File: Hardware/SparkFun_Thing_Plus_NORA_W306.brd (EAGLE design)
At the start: 22.9 x 58.4 mm, 155 parts, among them J1 THING_PLUS_LOGICAL, J2 LiPo, J3 QWIIC_RA, J4 MICRO-SDFRICTION, J5 USB-C, J6 SWD (DNP), Q1 3.1A/30V/105mΩ, Q2 MBT3904DW1T1, U1 UBLOX_NORA_W306, U3 XC6222B331MR-G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

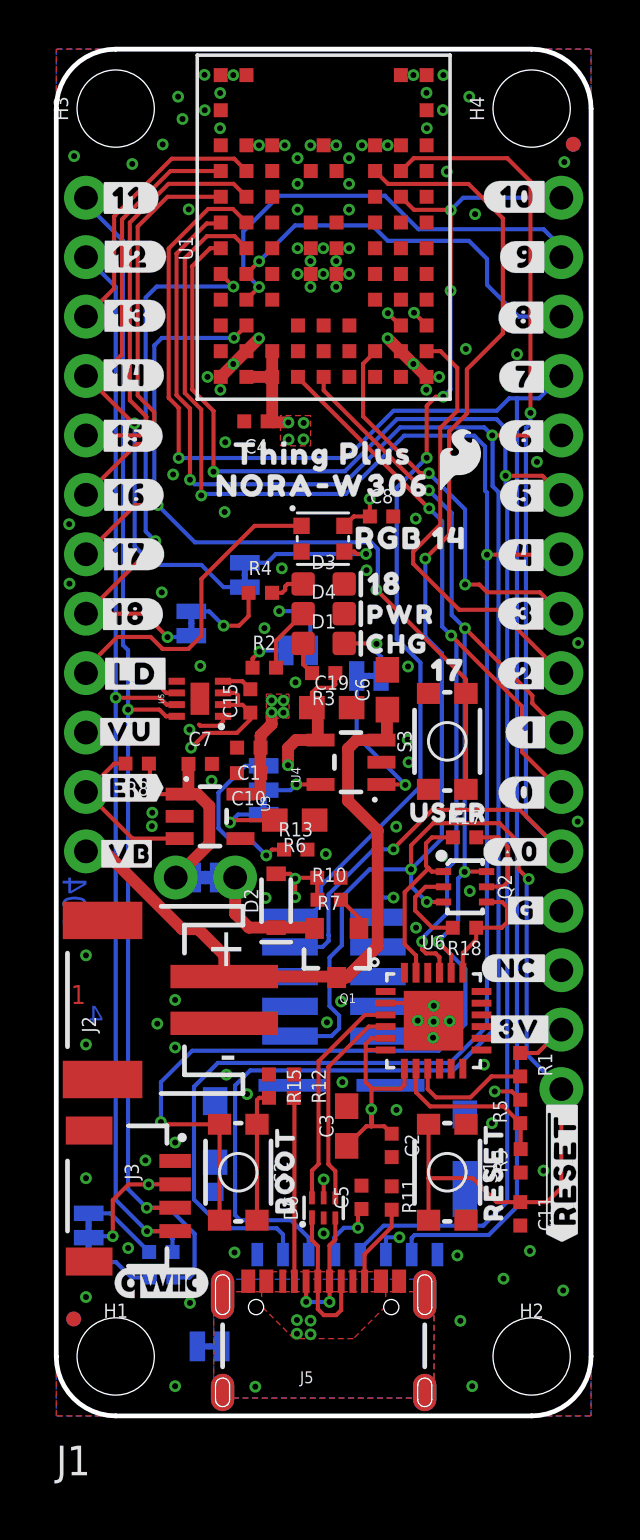
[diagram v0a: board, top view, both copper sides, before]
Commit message: Moved SDA/SCL from inner to bottom layer
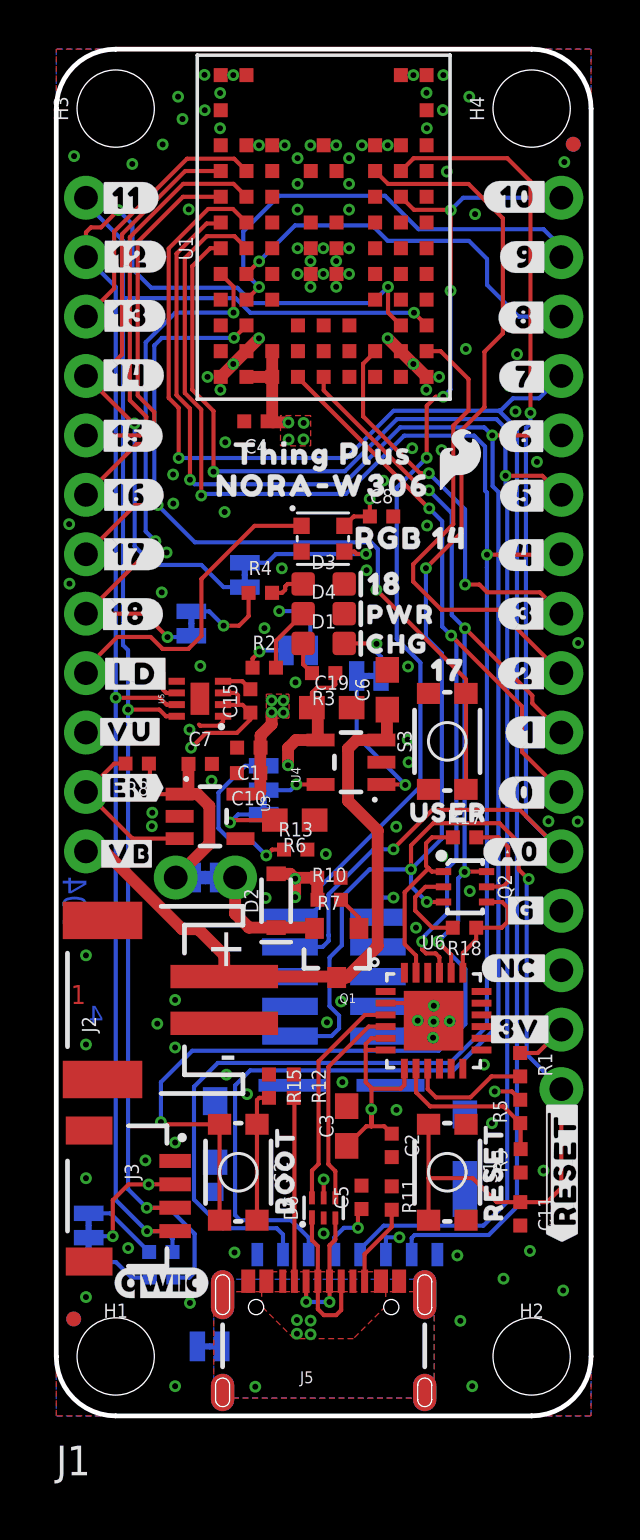
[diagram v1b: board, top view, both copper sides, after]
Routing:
- net PA26/SDA: track 70.6 -> 66.3 mm
- net PA25/SCL: track 63.5 -> 67.8 mm, vias 3 -> 4
- net PA30: track 19.0 -> 19.9 mm
- net GND: vias 118 -> 125

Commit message: Removed V_BUS plane on inner layer
To avoid splitting up the 3.3V plane on the inner layer, I decided to route V_USB (instead of using an additional separate plane).
Added some stitching traces/polys to stich up the 3.3V plane.
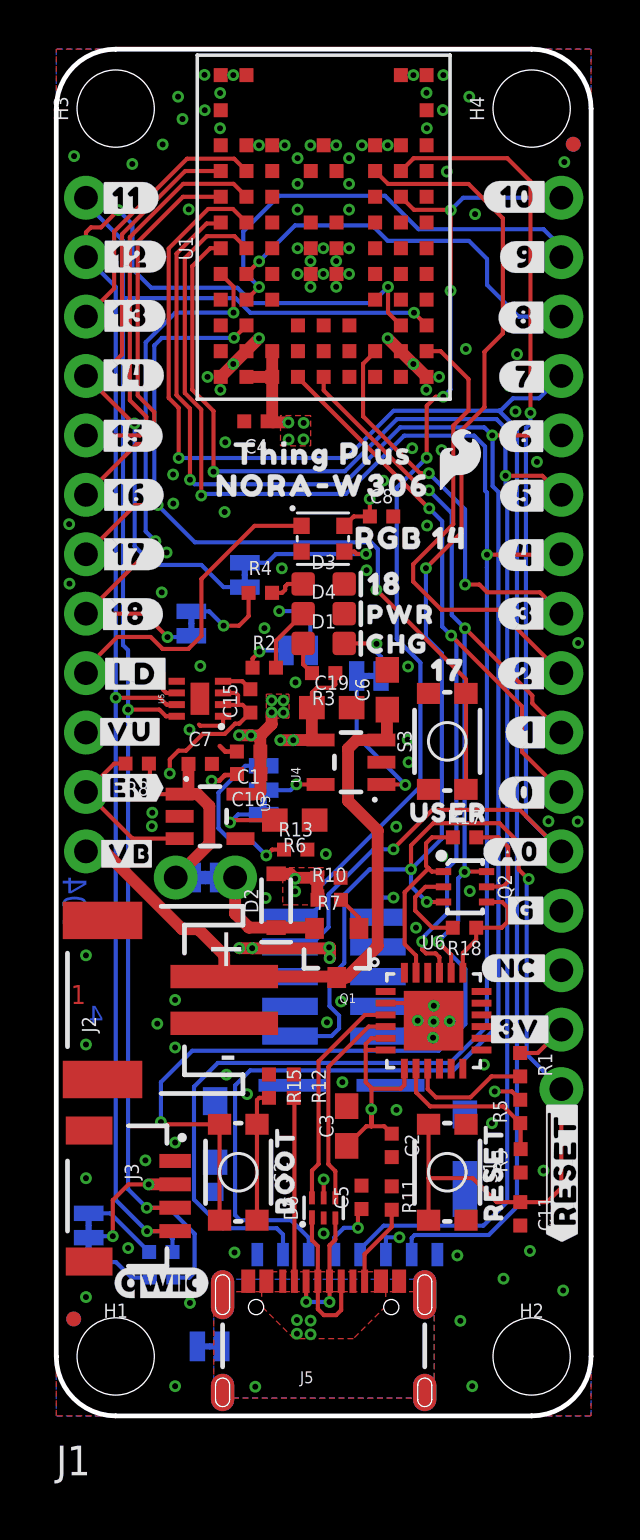
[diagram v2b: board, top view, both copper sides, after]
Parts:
- moved C1 0.17 mm to (8.22, 28.4)
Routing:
- net V_USB: track 19.8 -> 55.8 mm, vias 9 -> 10
- net 3.3V: track 46.3 -> 42.3 mm, vias 15 -> 21
- net GND: track 11.5 -> 13.6 mm

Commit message: Updated to new 0603 RED LED
-also updated the limiting resistor to correct value (4.7K) for DIO-17976
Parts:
- R2: value 1k -> 4.7k
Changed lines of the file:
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@@
 <setting verticaltext="up"/>
 </settings>
-<grid distance="0.05" unitdist="inch" unit="inch" style="lines" multiple="1" display="yes" altdistance="0.0001" altunitdist="inch" altunit="inch"/>
+<grid distance="0.05" unitdist="inch" unit="inch" style="lines" multiple="1" display="yes" altdistance="0.005" altunitdist="inch" altunit="inch"/>
 <layers>
 <layer number="1" name="Top" color="4" fill="1" visible="yes" active="yes"/>
@@
 <layer number="98" name="Guide" color="6" fill="1" visible="no" active="no"/>
 <layer number="99" name="SpiceOrder" color="7" fill="1" visible="no" active="no"/>
-<layer number="100" name="Muster" color="7" fill="1" visible="no" active="yes"/>
+<layer number="100" name="Muster" color="7" fill="1" visible="yes" active="yes"/>
 <layer number="101" name="Patch_Top" color="12" fill="4" visible="no" active="no"/>
 <layer number="102" name="Vscore" color="7" fill="1" visible="no" active="no"/>
@@
 <attribute name="VALUE" x="6.5532" y="4.1148" size="0.6096" layer="28" font="vector" ratio="20" rot="MR180" align="top-center"/>
 </element>
-<element name="R2" library="SparkFun-Resistors" package="0402-TIGHT" value="1k" x="8.89" y="31.981140625" smashed="yes">
+<element name="R2" library="SparkFun-Resistors" package="0402-TIGHT" value="4.7k" x="8.89" y="31.981140625" smashed="yes">
 <attribute name="NAME" x="8.89" y="32.743140625" size="0.6096" layer="25" font="vector" ratio="20" align="bottom-center"/>
-<attribute name="PROD_ID" value="RES-14342" x="8.89" y="31.981140625" size="1.778" layer="27" font="vector" ratio="15" display="off"/>
-<attribute name="VALUE" value="1k" x="8.89" y="31.219140625" size="0.6096" layer="27" font="vector" ratio="20" align="top-center"/>
+<attribute name="PROD_ID" value="RES-15343" x="8.89" y="31.981140625" size="1.778" layer="27" font="vector" ratio="15" display="off"/>
+<attribute name="VALUE" value="4.7k" x="8.89" y="31.219140625" size="0.6096" layer="27" font="vector" ratio="20" align="top-center"/>
 </element>
 <element name="LED" library="SparkFun-Jumpers" package="SMT-JUMPER_2_NC_TRACE_SILK" package3d_urn="urn:adsk.eagle:package:39281/1" value="" x="10.337803125" y="32.720278125" smashed="yes" rot="MR0">
@@
 <element name="D4" library="SparkFun-LED" package="LED-0603" value="RED" x="11.43" y="34.29" smashed="yes">
 <attribute name="NAME" x="11.43" y="34.925" size="0.6096" layer="25" font="vector" ratio="20" align="bottom-center"/>
-<attribute name="PROD_ID" value="DIO-00819" x="11.43" y="34.29" size="1.778" layer="27" font="vector" ratio="15" display="off"/>
-<attribute name="VALUE" x="11.43" y="33.655" size="0.6096" layer="27" font="vector" ratio="20" align="top-center"/>
+<attribute name="PROD_ID" value="DIO-17976" x="11.43" y="34.29" size="1.778" layer="27" font="vector" ratio="15" display="off"/>
 </element>
 <element name="U$23" library="output" package="PWR0" value="" x="14.72691875" y="34.25190625" smashed="yes"/>

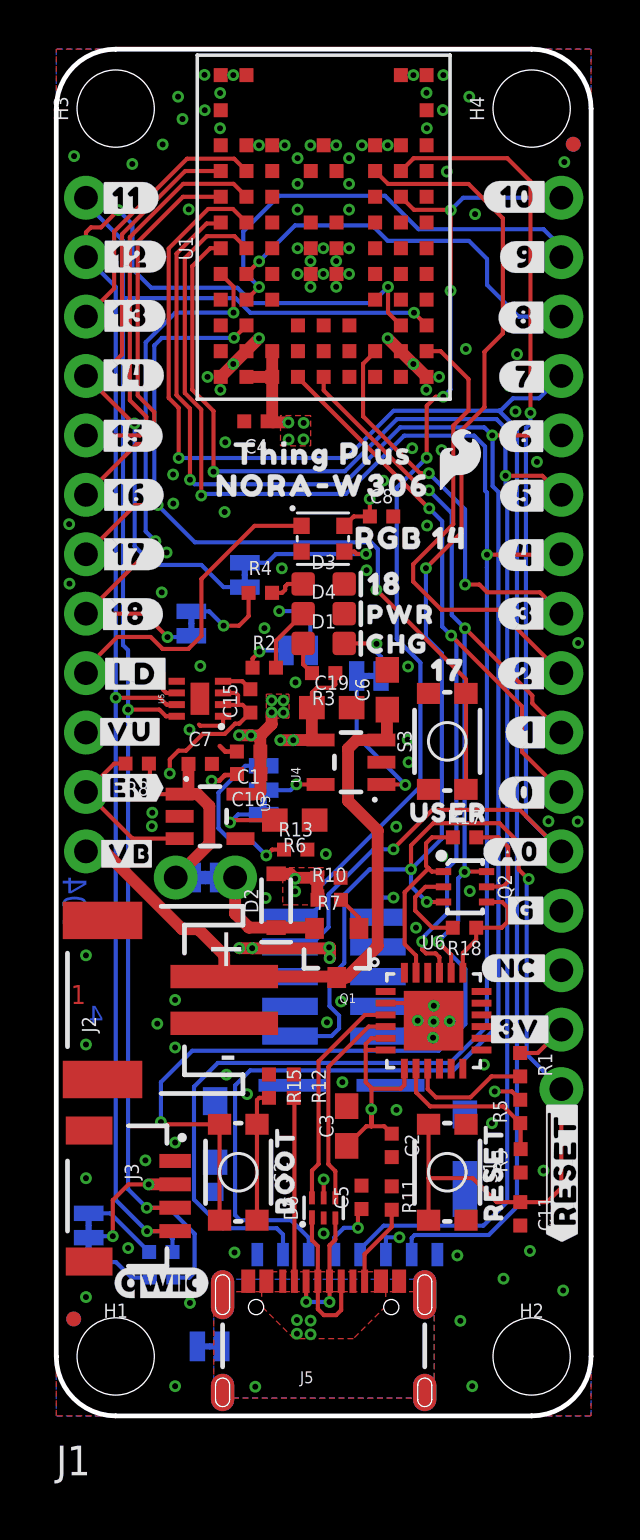
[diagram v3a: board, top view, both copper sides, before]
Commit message: Pre-group Review of v04 Changes
-moved logos to right box in SCH
-added column names to may pin mapping table in SCH
-adjusted SCH note about boot strapping pin internal pullups
-"single-cell" lipo batt note moved to single line
-changed current jumper silk to be "CUR"
-changed MEAS to smaller size and flat ends to fit better
-Adjusted V_BATT trace on inner layer to be 90 degreees when crossing the I2C lines
-Nudges trace off of user button for better gnd flow, added via nearby
-Added GND trace off of GND pad on fuel guage IC
-Nudges I2C vias near Fuel guage IC for better ground flow. added gnd vias nearby
-Nudges trace under charge IC for better gnd flow
-Larger SFE logo on top silk
-Larger OSHW logo on back
-Larger product name text on bottom silk
-updated NORA-w306 trestrict to rectangels rather than polys
-added silk lines to help populate close small passives
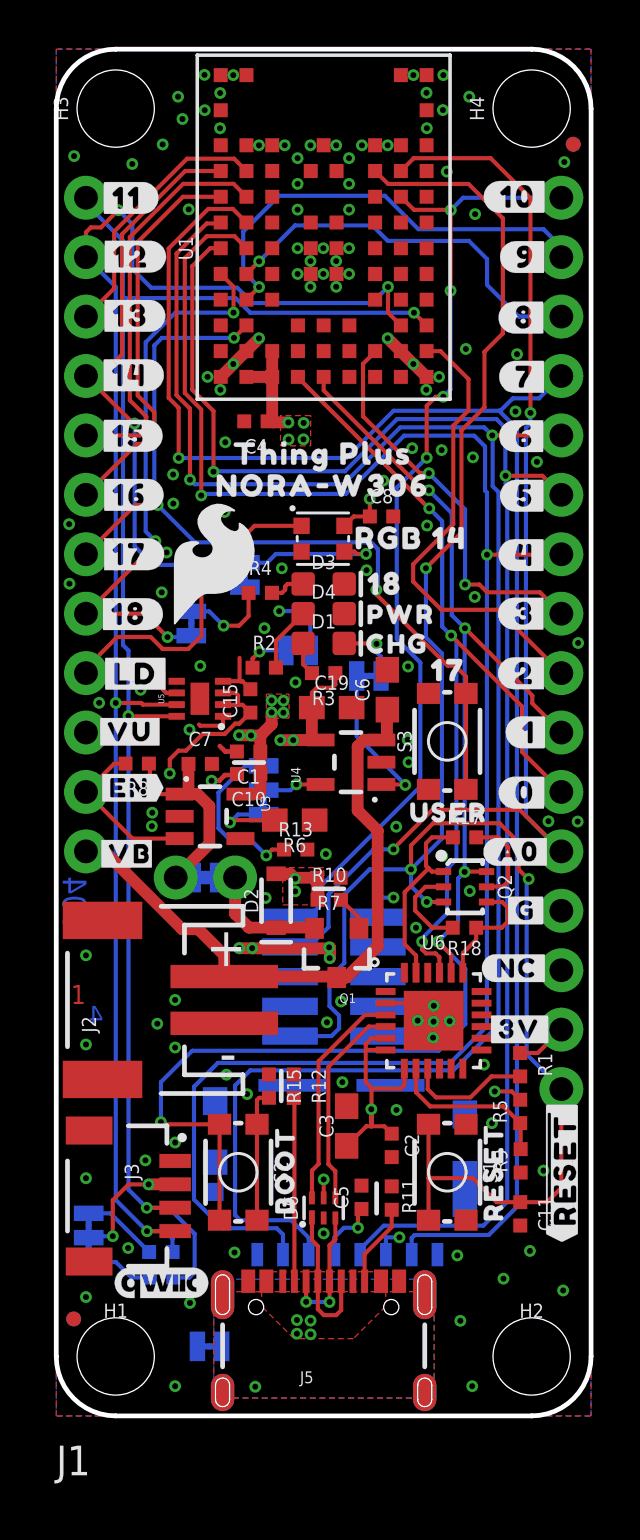
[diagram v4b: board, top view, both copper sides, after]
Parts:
- removed U$10: (no value), output:THING_PLUS_0
- removed U$6: (no value), output:NORA#W3060
- added U$27: (no value), output:CUR1714141837
- added U$28: (no value), output:NORA#W3061714141840
- LOGO2: value OSHW-LOGOMINI -> OSHW-LOGOM; device SparkFun-Aesthetics:OSHW-LOGO-MINI -> SparkFun-Aesthetics:OSHW-LOGO-M
- U$25: device output:#MEAS#1714141834 -> output:THING_PLUS1714141839
- U$3: device output:CHG0 -> output:#MEAS#1714141838
- U$8: device SparkFun-Aesthetics:SFE_LOGO_FLAME_.1 -> SparkFun-Aesthetics:SFE_LOGO_FLAME_.2
- moved U$25 35.6 mm to (11.3, 56.7)
- moved U$8 11.4 mm to (6.75, 36.4)
- moved U$3 7.39 mm to (6.34, 21.5), turned to 0 degrees
- moved U$19 5.87 mm to (12.5, 50.7)
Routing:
- net GND: track 13.6 -> 14.6 mm, vias 125 -> 128
- net V_BATT: track 40.1 -> 40.9 mm

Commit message: more tweaks pre-review
-added another ground via near I2C lines NW corner
-Added GND trace to connect GND near user button
-fixed some airwires caused by the new trestrict rectangles. Just routed the "missing" GND connections.
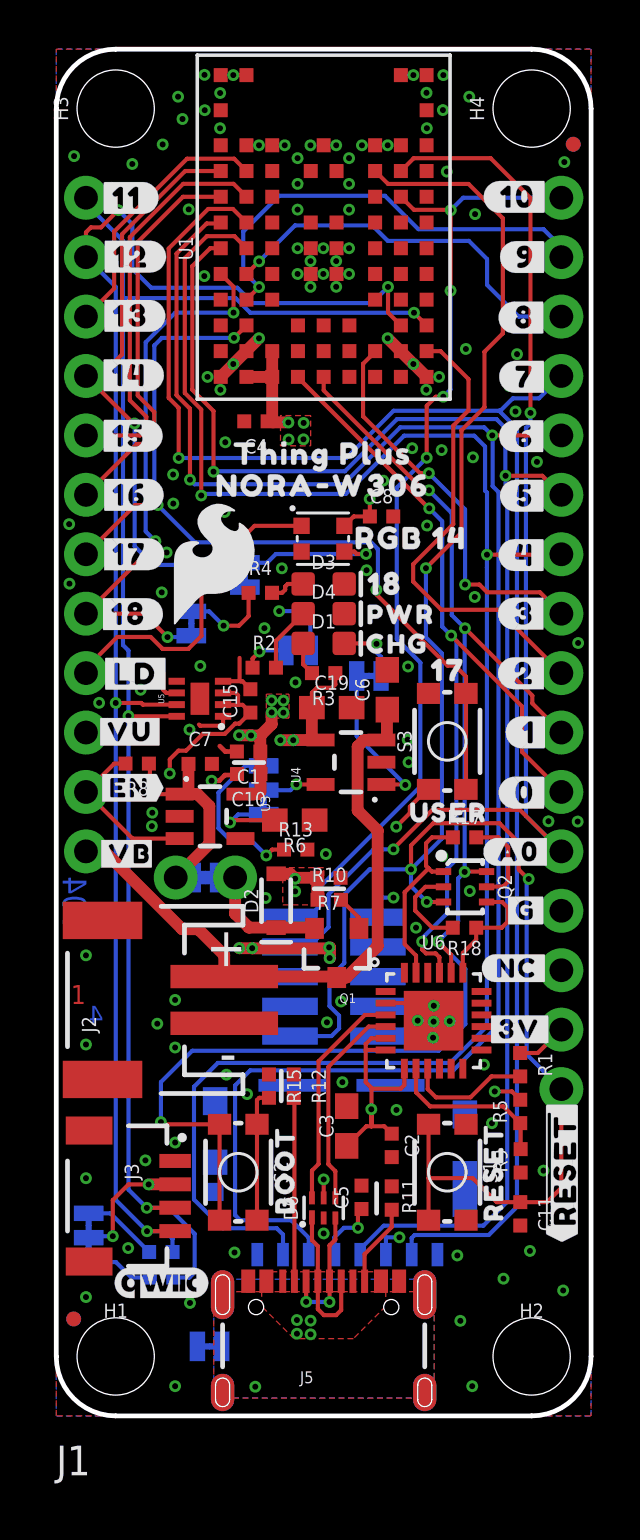
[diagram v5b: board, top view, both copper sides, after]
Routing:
- net GND: track 14.6 -> 18.2 mm, vias 128 -> 129
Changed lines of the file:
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@@
 <via x="3.6068" y="31.0388" extent="1-16" drill="0.254"/>
 <via x="1.831340625" y="30.48" extent="1-16" drill="0.254"/>
-<wire x1="15.265478125" y1="57.311459375" x2="14.73" y2="57.311" width="0" layer="19" extent="1-1"/>
-<wire x1="8.13" y1="57.311" x2="7.565478125" y2="57.311459375" width="0" layer="19" extent="1-1"/>
+<wire x1="14.531340625" y1="25.1841" x2="15.115540625" y2="25.7683" width="0.1778" layer="1"/>
+<wire x1="15.115540625" y1="25.7683" x2="15.115540625" y2="26.04008125" width="0.1778" layer="1"/>
+<wire x1="15.115540625" y1="26.04008125" x2="15.857" y2="26.781540625" width="0.1778" layer="1"/>
+<wire x1="15.857" y1="26.781540625" x2="15.9132" y2="26.781540625" width="0.1778" layer="1"/>
+<via x="6.3271375" y="48.719740625" extent="1-16" drill="0.254"/>
+<wire x1="15.265478125" y1="57.311459375" x2="15.26501875" y2="57.311" width="0.1778" layer="1"/>
+<wire x1="15.26501875" y1="57.311" x2="15.118078125" y2="57.311" width="0.1778" layer="1"/>
+<wire x1="15.118078125" y1="57.311" x2="15.1185375" y2="57.311459375" width="0.1778" layer="1"/>
+<wire x1="15.1185375" y1="57.311459375" x2="15.265478125" y2="57.311459375" width="0.1778" layer="1"/>
+<wire x1="14.73" y1="57.311" x2="14.730459375" y2="57.311459375" width="0.1778" layer="1"/>
+<wire x1="14.730459375" y1="57.311459375" x2="15.265478125" y2="57.311459375" width="0.1778" layer="1"/>
+<wire x1="8.13" y1="57.311" x2="7.5659375" y2="57.311" width="0.1778" layer="1"/>
+<wire x1="7.5659375" y1="57.311" x2="7.565478125" y2="57.311459375" width="0.1778" layer="1"/>
 </signal>
 <signal name="V_USB">
